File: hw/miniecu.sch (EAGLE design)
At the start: 3 parts

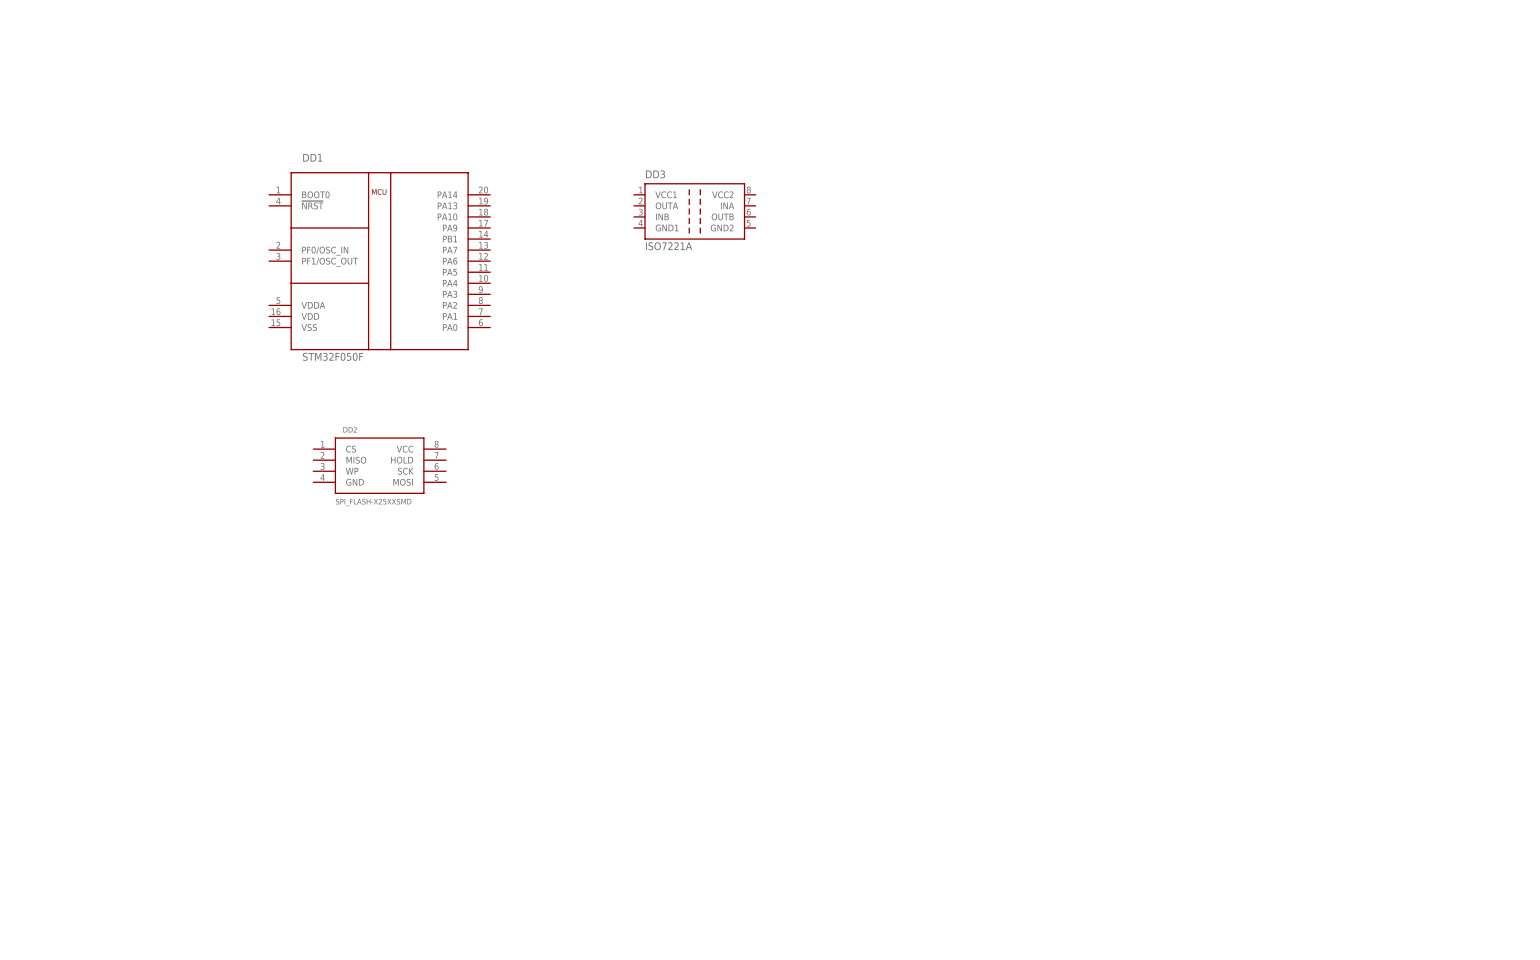
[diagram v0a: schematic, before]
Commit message: add isolator, esd lib
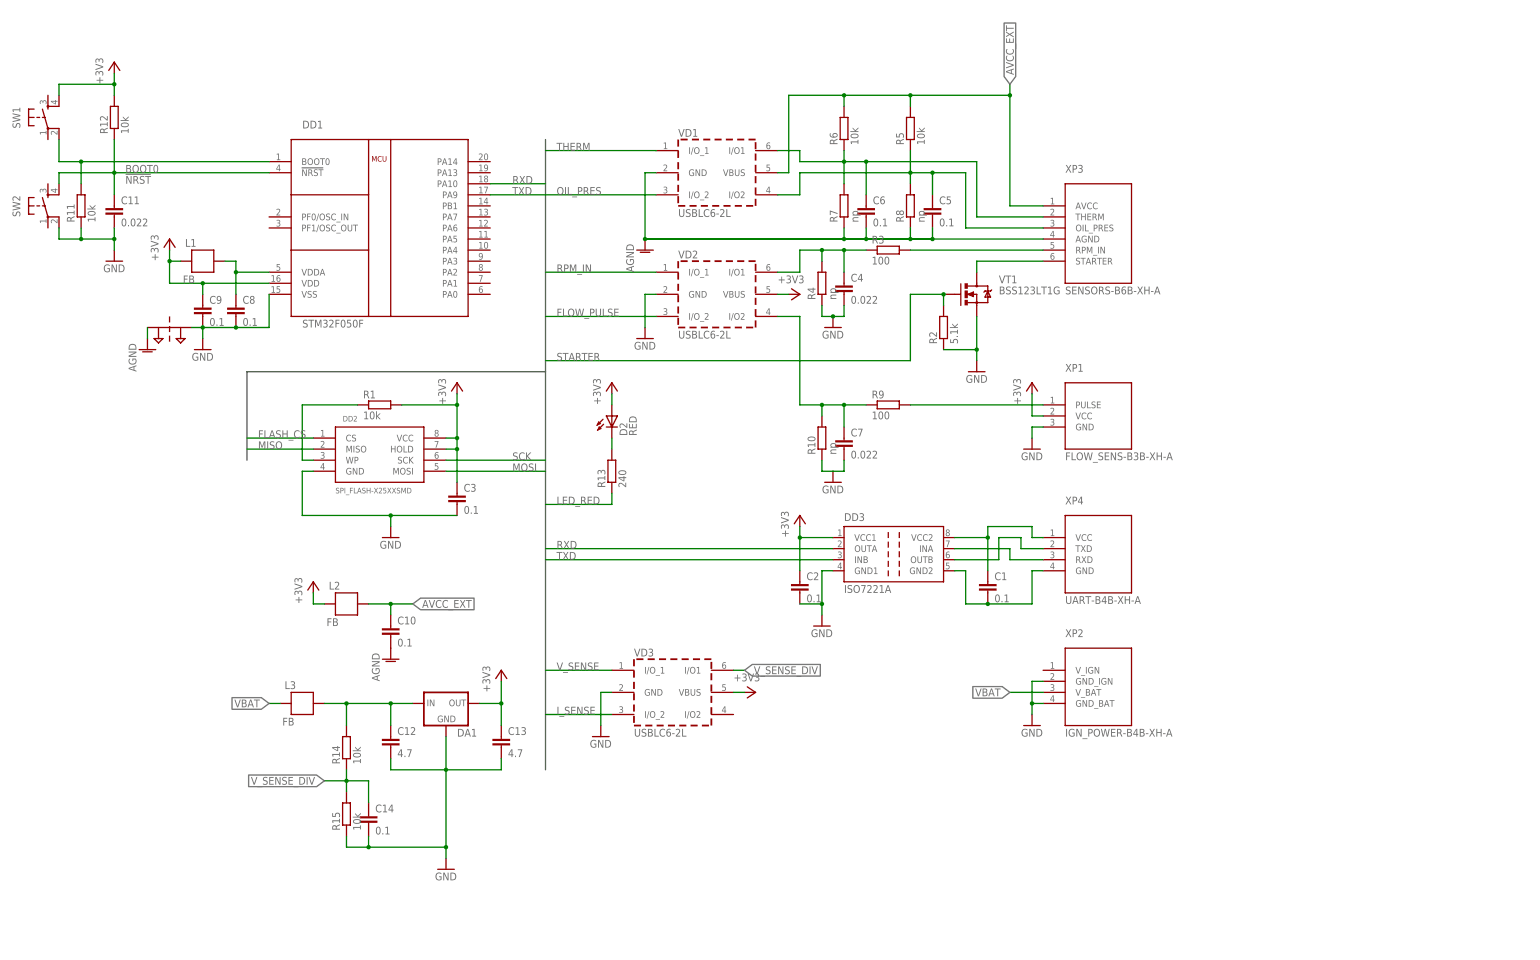
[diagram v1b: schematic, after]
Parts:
- added C1, C10, C14, C2, C3, C5, C6, C8, C9: 0.1, resistor:C-EUC0603
- added C11: 0.022, resistor:C-EUC0805
- added C12, C13: 4.7, resistor:C-EUC0805
- added C4, C7: 0.022, resistor:C-EUC0603
- added D2: RED, SparkFun-LED:LED-RED0603
- added DA1: (no value), power-ic:MCP1700SOT-23
- added L1, L2, L3: FB, SparkFun-Passives:FB
- added PT1: 2PT_GND_TIE, SparkFun-Passives:2PT_GND_TIE
- added R1: 10k, resistor:R-EU_R0603
- added R10, R4: np, resistor:R-EU_R0603
- added R11, R12, R14, R15, R5, R6: 10k, resistor:R-EU_R0805
- added R13: 240, resistor:R-EU_R0603
- added R2: 5.1k, resistor:R-EU_R0603
- added R3, R9: 100, resistor:R-EU_R0603
- added R7, R8: np, resistor:R-EU_R0805
- added SW1, SW2: (no value), SparkFun-Electromechanical:TAC_SWITCHSMD
- added VD1, VD2, VD3: USBLC6-2L, usblc6:USBLC6-2SC6
- added VT1: BSS123LT1G, SparkFun-DiscreteSemi:MOSFET-NCHANNELBSS123LT1G
- added XP1: FLOW_SENS-B3B-XH-A, miniecu-con:FLOW_SENS-B3B-XH-A
- added XP2: IGN_POWER-B4B-XH-A, miniecu-con:IGN_POWER-B4B-XH-A
- added XP3: SENSORS-B6B-XH-A, miniecu-con:SENSORS-B6B-XH-A
- added XP4: UART-B4B-XH-A, miniecu-con:UART-B4B-XH-A
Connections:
- new net !NRST: C11.1, R12.1, SW2.4
- new net +3V3: C13.1, C2.1, C3.1, C9.1, D2.A, DA1.OUT, DD1.VDD, DD2.HOLD, DD2.VCC, DD3.VCC1, L1.P$2, L2.P$2, R1.2, R12.2, SW1.4, VD2.VBUS, VD3.VBUS, XP1.VCC
- new net AGND: C10.2, C5.2, C6.2, PT1.P$1, R7.1, R8.1, VD1.GND, XP3.AGND
- new net AVCC_EXT: C10.1, L2.P$1, R5.2, R6.2, VD1.VBUS, XP3.AVCC
- new net BOOT0: R11.2, SW1.2
- new net FLASH_CS: DD2.CS
- new net FLOW_PULSE: C7.1, R10.2, R9.1, VD2.I/O2, VD2.I/O_2
- new net GND: C11.2, C12.2, C13.2, C14.2, C2.2, C3.2, C4.2, C7.2, C8.2, C9.2, DA1.GND, DD1.VSS, DD2.GND, DD3.GND1, PT1.P$2, R10.1, R11.1, R15.1, R2.1, R4.1, SW2.2, VD2.GND, VD3.GND, VT1.S, XP1.GND, XP2.GND_BAT, XP2.GND_IGN
- new net GND2: C1.2, DD3.GND2, XP4.GND
- new net IORXD: DD3.INA, XP4.RXD
- new net IOTXD: DD3.OUTB, XP4.TXD
- new net I_SENSE: VD3.I/O_2
- new net LED_RED: R13.1
- new net MISO: DD2.MISO
- new net MOSI: DD2.MOSI
- new net N$1: C8.1, DD1.VDDA, L1.P$1
- new net N$2: D2.C, R13.2
- new net N$3: DD2.WP, R1.1
- new net N$4: R9.2, XP1.PULSE
- new net N$5: R3.2, XP3.RPM_IN
- new net N$6: C12.1, DA1.IN, L3.P$1, R14.2
- new net OIL_PRES: C5.1, R5.1, R8.2, VD1.I/O2, VD1.I/O_2, XP3.OIL_PRES
- new net RPM_IN: C4.1, R3.1, R4.2, VD2.I/O1, VD2.I/O_1
- new net RXD: DD1.PA10, DD3.OUTA
- new net SCK: DD2.SCK
- new net STARTER: R2.2, VT1.G
- new net STARTER_OUT: VT1.D, XP3.STARTER
- new net THERM: C6.1, R6.1, R7.2, VD1.I/O1, VD1.I/O_1, XP3.THERM
- new net TXD: DD1.PA9, DD3.INB
- new net VBAT: L3.P$2, XP2.V_BAT
- new net VCC2: C1.1, DD3.VCC2, XP4.VCC
- new net V_SENSE: VD3.I/O_1
- new net V_SENSE_DIV: C14.1, R14.1, R15.2, VD3.I/O1
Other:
- moved on the sheet: DD1, DD2, DD3

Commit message: first schematic.
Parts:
- removed D2: RED, SparkFun-LED:LED-RED0603
- added C15: 0.1, resistor:C-EUC0603
- added DA2: VN5E025AJ-E, power-ic:VN5E025AJ-E
- added HL1: KAA-3528ESGC, led2:KAA-3528ESGC
- added R16, R19: 10k, resistor:R-EU_R0805
- added R17: np, resistor:R-EU_R0805
- added R18: 5.1k, resistor:R-EU_R0603
- added U$1: CREATIVE_COMMONS_BY-SA, logo:CREATIVE_COMMONS_BY-SA
- C1: value 0.1 -> 0.022; device resistor:C-EUC0603 -> resistor:C-EUC0805
- C11: device resistor:C-EUC0805 -> resistor:C-EUC0603
- C12: value 4.7 -> 0.022; device resistor:C-EUC0805 -> resistor:C-EUC0603
- C13: value 4.7 -> 0.1; device resistor:C-EUC0805 -> resistor:C-EUC0603
- C4, C7: value 0.022 -> 0.1
- C6, C8: value 0.1 -> 4.7; device resistor:C-EUC0603 -> resistor:C-EUC0805
- R1: device resistor:R-EU_R0603 -> resistor:R-EU_R0805
- R11: value 10k -> np; device resistor:R-EU_R0805 -> resistor:R-EU_R0603
- R13: value 240 -> np; device resistor:R-EU_R0603 -> resistor:R-EU_R0805
- R14, R15: value 10k -> 100; device resistor:R-EU_R0805 -> resistor:R-EU_R0603
- R2: value 5.1k -> 10k; device resistor:R-EU_R0603 -> resistor:R-EU_R0805
- R3: value 100 -> 10k; device resistor:R-EU_R0603 -> resistor:R-EU_R0805
- R4: value np -> 10k; device resistor:R-EU_R0603 -> resistor:R-EU_R0805
- R5: device resistor:R-EU_R0805 -> resistor:R-EU_R0603
- R6: value 10k -> 140; device resistor:R-EU_R0805 -> resistor:R-EU_R0603
- R7: value np -> 10k
- R8: value np -> 100; device resistor:R-EU_R0805 -> resistor:R-EU_R0603
- R9: value 100 -> 10k
- XP1: value FLOW_SENS-B3B-XH-A -> SENSORS-B6B-XH-A; device miniecu-con:FLOW_SENS-B3B-XH-A -> miniecu-con:SENSORS-B6B-XH-A
- XP2: value IGN_POWER-B4B-XH-A -> FLOW_SENS-B3B-XH-A; device miniecu-con:IGN_POWER-B4B-XH-A -> miniecu-con:FLOW_SENS-B3B-XH-A
- XP3: value SENSORS-B6B-XH-A -> UART-B4B-XH-A; device miniecu-con:SENSORS-B6B-XH-A -> miniecu-con:UART-B4B-XH-A
- XP4: value UART-B4B-XH-A -> IGN_POWER-B4B-XH-A; device miniecu-con:UART-B4B-XH-A -> miniecu-con:IGN_POWER-B4B-XH-A
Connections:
- removed net LED_RED: R13.1
- removed net N$5: R3.2, XP3.RPM_IN
- removed net V_SENSE_DIV: C14.1, R14.1, R15.2, VD3.I/O1
- new net IGN_EN: DD1.PA14, R8.1
- new net LED: DD1.PF0/OSC_IN, R6.1
- new net N$7: DA2.INPUT, R8.2
- new net N$9: DA2.CS_DIS, R9.2
- new net RPM_IN_CON: R14.2, XP1.RPM_IN
- new net V_IGN: DA2.OUTPUT1, DA2.OUTPUT2, DA2.OUTPUT3, DA2.OUTPUT4, DA2.OUTPUT5, DA2.OUTPUT6, XP4.V_IGN
- net !NRST: now also C1.1, R2.1; no longer C11.1, R12.1
- net +3V3: now also C10.1, C7.1, C8.1, HL1G.A, L3.P$2, R19.2, R2.2, R5.2, VD1.VBUS, XP2.VCC; no longer C13.1, C3.1, C9.1, D2.A, L2.P$2, R1.2, R12.2, VD2.VBUS, XP1.VCC
- net AGND: now also C13.2, C14.2, R13.1, R17.1, VD2.GND, XP1.AGND; no longer C10.2, C6.2, R7.1, R8.1, VD1.GND, XP3.AGND
- net AVCC_EXT: now also C5.1, L3.P$1, R12.2, R16.2, VD2.VBUS, XP1.AVCC; no longer C10.1, L2.P$1, R5.2, R6.2, VD1.VBUS, XP3.AVCC
- net BOOT0: now also R1.2; no longer R11.2
- net FLASH_CS: now also DD1.PF1/OSC_OUT
- net FLOW_PULSE: now also C12.1, DD1.PB1, R11.2, R15.1, VD3.I/O2, VD3.I/O_2; no longer C7.1, R10.2, R9.1, VD2.I/O2, VD2.I/O_2
- net GND: now also C1.2, C10.2, C6.2, DA2.GND, HL1R.C, R1.1, R18.1, R7.2, R9.1, VD1.GND, XP2.GND, XP4.GND_BAT, XP4.GND_IGN; no longer C13.2, C14.2, R15.1, R2.1, VD2.GND, XP1.GND, XP2.GND_BAT, XP2.GND_IGN
- net GND2: now also C15.2, XP3.GND; no longer C1.2, XP4.GND
- net IORXD: now also XP3.RXD; no longer XP4.RXD
- net IOTXD: now also XP3.TXD; no longer XP4.TXD
- net I_SENSE: now also C9.1, DA2.CURRENT_SENSE, DD1.PA2, R7.1, VD1.I/O2, VD1.I/O_2; no longer VD3.I/O_2
- net MISO: now also DD1.PA6
- net MOSI: now also DD1.PA7
- net N$1: now also C3.1; no longer C8.1
- net N$2: now also HL1G.C, HL1R.A, R6.2; no longer D2.C, R13.2
- net N$3: now also R5.1; no longer R1.1
- net N$4: now also R15.2, R19.1, XP2.PULSE; no longer R9.2, XP1.PULSE
- net N$6: now also C6.1, L2.P$1, R3.2; no longer C12.1, L3.P$1, R14.2
- net OIL_PRES: now also C14.1, DD1.PA4, R16.1, R17.2, VD2.I/O2, VD2.I/O_2, XP1.OIL_PRES; no longer C5.1, R5.1, R8.2, VD1.I/O2, VD1.I/O_2, XP3.OIL_PRES
- net RPM_IN: now also C11.1, DD1.PA1, R10.2, R14.1, VD3.I/O1, VD3.I/O_1; no longer C4.1, R3.1, R4.2, VD2.I/O1, VD2.I/O_1
- net SCK: now also DD1.PA5
- net STARTER: now also DD1.PA13, R18.2; no longer R2.2
- net STARTER_OUT: now also XP1.STARTER; no longer XP3.STARTER
- net THERM: now also C13.1, DD1.PA0, R12.1, R13.2, VD2.I/O1, VD2.I/O_1, XP1.THERM; no longer C6.1, R6.1, R7.2, VD1.I/O1, VD1.I/O_1, XP3.THERM
- net VBAT: now also DA2.VCC1, DA2.VCC2, DA2.VCC_TAB, L2.P$2, XP4.V_BAT; no longer L3.P$2, XP2.V_BAT
- net VCC2: now also C15.1, XP3.VCC; no longer C1.1, XP4.VCC
- net V_SENSE: now also C4.1, DD1.PA3, R3.1, R4.2, VD1.I/O1, VD1.I/O_1; no longer VD3.I/O_1
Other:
- moved on the sheet: C1, C10, C11, C12, C13, C14, C2, C3, C4, C5, C6, C7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

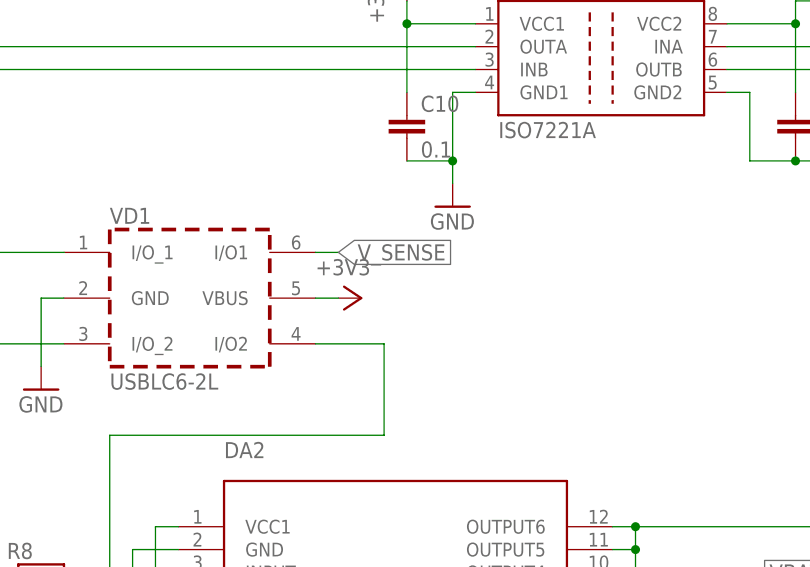
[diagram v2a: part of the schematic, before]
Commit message: change iv esd supply +3V3->AVCC
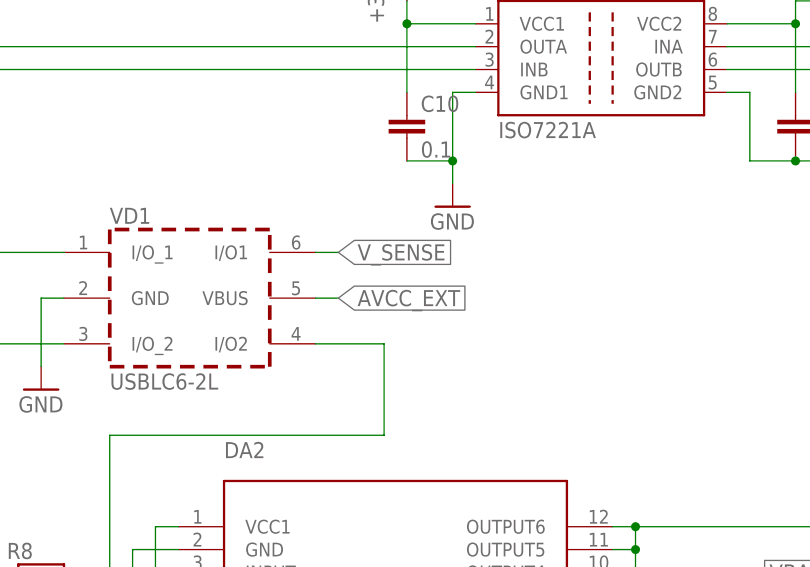
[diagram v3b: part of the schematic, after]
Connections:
- net +3V3: no longer VD1.VBUS
- net AVCC_EXT: now also VD1.VBUS
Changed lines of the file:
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@@
 <part name="VD1" library="usblc6" deviceset="USBLC6-2" device="SC6" value="USBLC6-2L"/>
 <part name="GND12" library="supply1" deviceset="GND" device=""/>
-<part name="+3V10" library="supply1" deviceset="+3V3" device=""/>
 <part name="DA2" library="power-ic" deviceset="VN5E025AJ" device="-E"/>
 <part name="R8" library="resistor" deviceset="R-EU_" device="R0603" value="100"/>
@@
 <instance part="VD1" gate="G$1" x="78.74" y="-101.6"/>
 <instance part="GND12" gate="1" x="53.34" y="-104.14"/>
-<instance part="+3V10" gate="G$1" x="88.9" y="-93.98" rot="R270"/>
 <instance part="DA2" gate="G$1" x="88.9" y="-137.16"/>
 <instance part="R8" gate="G$1" x="53.34" y="-124.46"/>
@@
 <label x="5.08" y="-78.74" size="1.778" layer="95" xref="yes"/>
 <junction x="0" y="-78.74"/>
+</segment>
+<segment>
+<pinref part="VD1" gate="G$1" pin="VBUS"/>
+<wire x1="83.82" y1="-93.98" x2="86.36" y2="-93.98" width="0.1524" layer="91"/>
+<label x="86.36" y="-93.98" size="1.778" layer="95" xref="yes"/>
 </segment>
 </net>
@@
 </segment>
 <segment>
-<pinref part="VD1" gate="G$1" pin="VBUS"/>
-<pinref part="+3V10" gate="G$1" pin="+3V3"/>
-<wire x1="86.36" y1="-93.98" x2="83.82" y2="-93.98" width="0.1524" layer="91"/>
-</segment>
-<segment>
